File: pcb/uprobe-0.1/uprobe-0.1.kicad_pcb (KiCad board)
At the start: 4 copper layers, 33.5 x 77 mm, 107 parts, among them J1 uConsoleEXT, J2 Conn_02x05_Odd_Even, J3 Conn_02x05_Odd_Even, J4 JST_SH_BM03B-SRSS, J5 Conn_01x02, J7 Conn_01x04, Q1 BSS138, Q7 DMG1024UV, Q8 DMG1023UV, SW1 XUNPU TS-1088-AR02016, SW2 XUNPU TS-1088-AR02016, U1 ATmega8A-M, U10 74LVC2T45DC, U11 74LVC2T45DC, U12 74LVC2T45DC, U2 AMS1117-3.3, U3 AP22653, U4 AP22653, U5 STM32F103CBUx, U6 74LVC2T45DC, U7 74LVC2T45DC, U8 74LVC2T45DC, U9 74LVC2T45DC, Y1 ABM8-12.000MHZ-B2-T, Y2 ABM8-8.000MHZ-B2-T

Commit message: silkscreen
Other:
- board text added: "5V"
- board text added: "BMP flash"
- board text added: "GND"
- board text added: "RST"
- board text added: "SWCLK"
- board text added: "SWD/JTAG"
- board text added: "SWDIO"
- board text added: "TX GND RX"
- board text added: "UART"
- board text added: "USBASP"
- board text added: "bridge these for"
- board text added: "unified connector"
- board text removed: "swd/jtag"
- board text removed: "uart"
- board text removed: "usbasp"

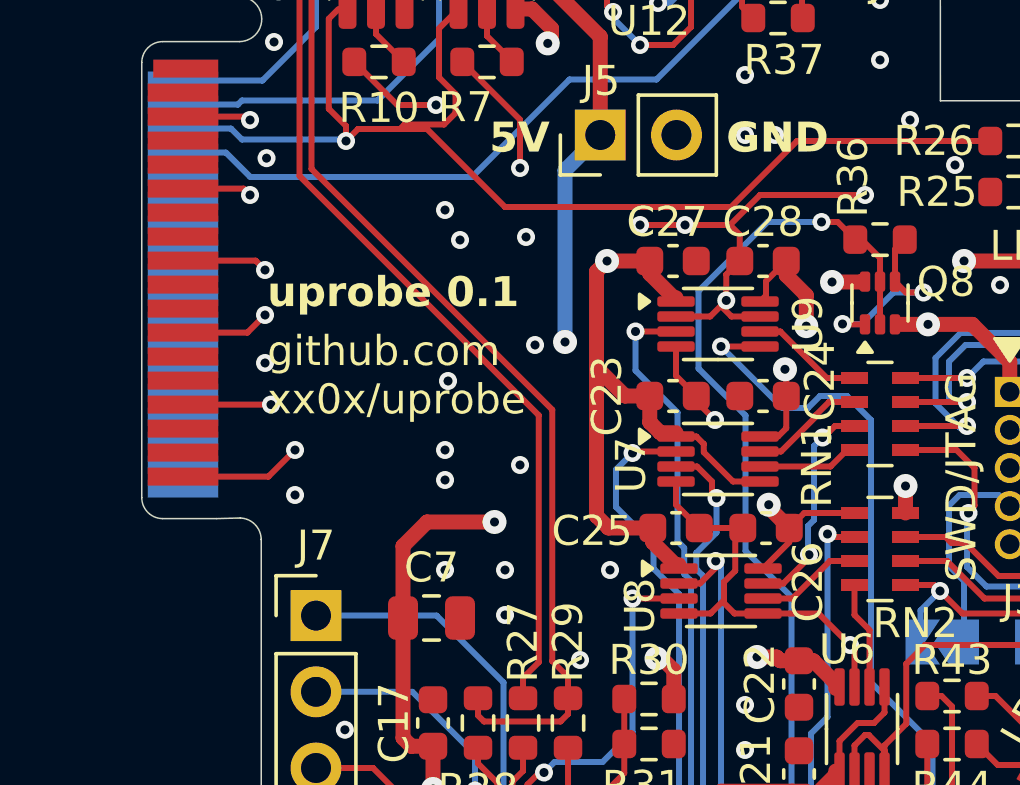
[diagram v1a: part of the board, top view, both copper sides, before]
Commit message: additional gpio
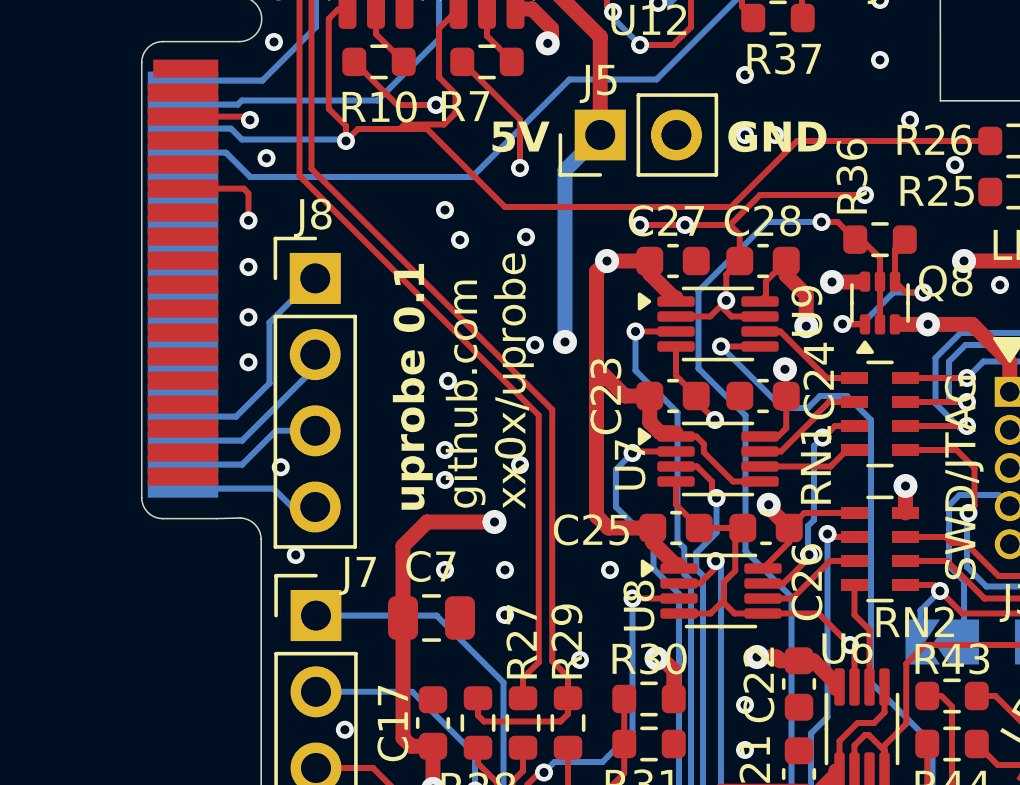
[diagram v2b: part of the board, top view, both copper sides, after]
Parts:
- added J8: Conn_01x04, Connector_PinHeader_2.54mm:PinHeader_1x04_P2.54mm_Vertical, F.Cu at (125.7, 105.8)
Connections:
- J1 pad 46: unconnected-(J1-GPIO42-Pad46) -> Net-(J1-GPIO42)
- J1 pad 48: unconnected-(J1-GPIO43-Pad48) -> Net-(J1-GPIO43)
- J1 pad 50: unconnected-(J1-GPIO44-Pad50) -> Net-(J1-GPIO44)
- J1 pad 52: unconnected-(J1-GPIO45-Pad52) -> Net-(J1-GPIO45)
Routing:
- net GND: track 219.2 -> 207.3 mm, vias 112 -> 111
- net Net-(J1-GPIO42): track 0.00 -> 7.50 mm
- net Net-(J1-GPIO43): track 0.00 -> 5.85 mm
- net Net-(J1-GPIO44): track 0.00 -> 4.88 mm
- net Net-(J1-GPIO45): track 0.00 -> 4.66 mm
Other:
- board text added: "42"
- board text added: "43"
- board text added: "44"
- board text added: "45"
- board text added: "GPIO"
